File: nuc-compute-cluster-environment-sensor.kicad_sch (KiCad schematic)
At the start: 121 parts, among them J1 USB4105-GF-A, J2 SM04B-SRSS-TB-LF-SN, J3 SM04B-SRSS-TB-LF-SN, U1 FT4232H-56Q, U2 AP7370-33SA-7, U3 STM32G474CET6, U4 MB85RC1MTPNF-G, U5 SHT45, U6 BME280, Y1 ABM3B-12.000MHZ-B2-T, Y2 ECS-_327-12_5-34B-TR, Y3 ABM3B-8.000MHZ-10-1-U-T

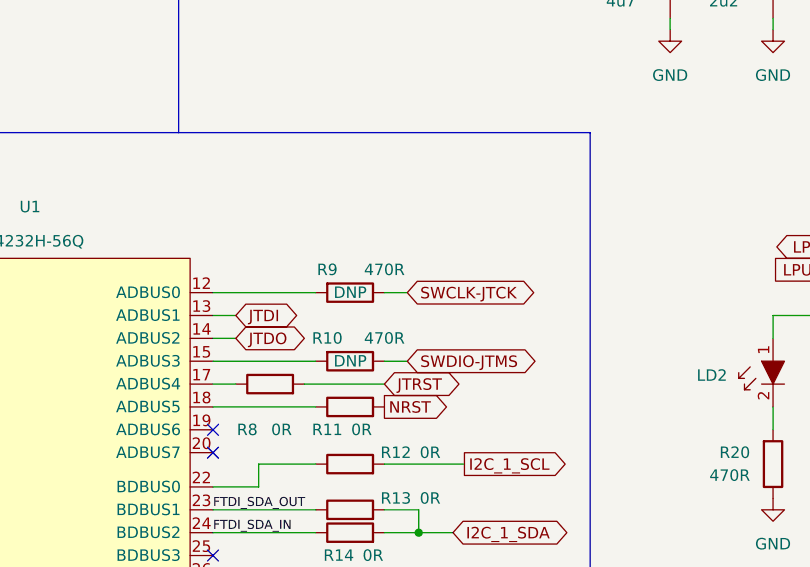
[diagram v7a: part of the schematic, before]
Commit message: Fixed connection of SWD/JTAG configuration resistors
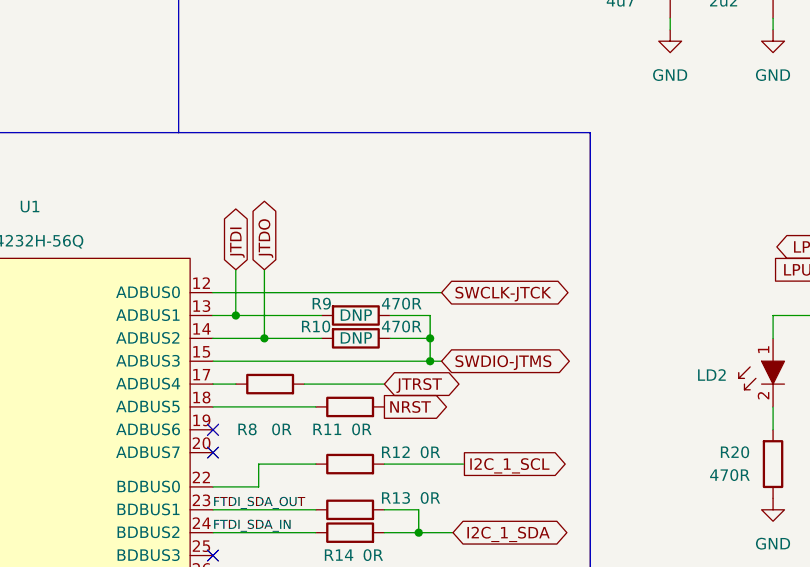
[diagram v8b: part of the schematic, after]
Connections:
- net JTDI: now also R9.2
- net JTDO: now also R10.2
- net SWCLK-JTCK: now also U1.12 (ADBUS0); no longer R9.1
- net SWDIO-JTMS: now also R9.1, U1.15 (ADBUS3)
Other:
- moved on the sheet: R10, R9
